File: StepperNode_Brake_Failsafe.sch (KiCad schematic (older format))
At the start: 2 parts

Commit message: Added Aux Prop Interface Sheet
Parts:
- added P?: CONN_01X02_2XMNT, symbol CONN_01X02_2XMNT
- added Q?: Q_NMOS_DGS, symbol Q_NMOS_DGS
- added RL?: Relay_DPDT, symbol Relay_DPDT
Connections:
- net labels added: WDT_GOOD
- wire segments 2 -> 4
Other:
- note added: "Brake 2 G210x\nEnable Link"
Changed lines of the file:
@@
 $Descr A3 16535 11693
 encoding utf-8
-Sheet 14 14
+Sheet 14 16
 Title "Brake Failsafe Control"
 Date ""
@@
 Text Notes 9850 2800 0    60   ~ 0
 G210x Active when\nRelay Energized
+$Comp
+L Q_NMOS_DGS Q?
+U 1 1 5753D96E
+P 8700 4250
+F 0 "Q?" H 9000 4300 50  0000 R CNN
+F 1 "Q_NMOS_DGS" H 9350 4200 50  0000 R CNN
+F 2 "" H 8900 4350 50  0000 C CNN
+F 3 "" H 8700 4250 50  0000 C CNN
+	1    8700 4250
+	1    0    0    -1
+$EndComp
+Text HLabel 6050 4200 0    60   Input ~ 0
+WDT_GOOD
+$Comp
+L CONN_01X02_2XMNT P?
+U 1 1 5753DAA1
+P 12200 5950
+F 0 "P?" H 12200 6100 50  0000 C CNN
+F 1 "CONN_01X02_2XMNT" V 12300 5950 50  0000 C CNN
+F 2 "" H 12200 5950 50  0000 C CNN
+F 3 "" H 12200 5950 50  0000 C CNN
+	1    12200 5950
+	1    0    0    -1
+$EndComp
+Text Notes 12550 5950 0    60   ~ 0
+Brake 2 G210x\nEnable Link
+$Comp
+L Relay_DPDT RL?
+U 1 1 5753DAA8
+P 9100 6450
+F 0 "RL?" H 9500 7250 60  0000 C CNN
+F 1 "Relay_DPDT" H 9500 6400 60  0000 C CNN
+F 2 "" H 9100 6450 60  0000 C CNN
+F 3 "" H 9100 6450 60  0000 C CNN
+	1    9100 6450
+	1    0    0    -1
+$EndComp
+Wire Wire Line
+	10100 6000 12000 6000
+Wire Wire Line
+	12000 5900 10100 5900
+Text Notes 9850 5500 0    60   ~ 0
+G210x Active when\nRelay Energized
 $EndSCHEMATC

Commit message: Netlist top level
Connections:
- net labels added: PUSH_INTLK_A, PUSH_INTLK_B
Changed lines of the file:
@@
 Text Notes 9850 5500 0    60   ~ 0
 G210x Active when\nRelay Energized
+Text HLabel 5550 5100 0    60   Input ~ 0
+PUSH_INTLK_A
+Text HLabel 5550 5200 0    60   Input ~ 0
+PUSH_INTLK_B
 $EndSCHEMATC

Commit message: Updated node core connector pages and added interlocks.
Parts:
- removed Q?: Q_NMOS_DGS, symbol Q_NMOS_DGS
- removed RL?: Relay_DPDT, symbol Relay_DPDT
- added D?: 1N4004, symbol D
- added U?: NUD3124LT1G, symbol NUD3124LT1G
- added U? (x2): 74LVC1G32GW,125, symbol 74LVC1G32GW,125
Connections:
- net labels added: GNDD
- wire segments 4 -> 20
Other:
- note added: "If WDT or any Interlock is active then\nThe drive controllers always remain active.\nIn this mode a WDT fault can't cause loss of drive motors."
- note added: "Output is high when either\nInterlock is on"
- note added: "The purpose of this function is to:\n1. Ensure that if the WDT_GOOD signal goes low the drive controllers do not drop out if the interlock is enabled.\n2. Loss of either 24VA or 24VB will not cause the loss of an individual drive controller."
- note added: "Todo:\nPower RLY from redundant source."
- moved on the sheet: P?, RL?
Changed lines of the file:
@@
 L CONN_01X02_2XMNT P?
 U 1 1 575559F0
-P 12200 3250
-F 0 "P?" H 12200 3400 50  0000 C CNN
-F 1 "CONN_01X02_2XMNT" V 12300 3250 50  0000 C CNN
-F 2 "" H 12200 3250 50  0000 C CNN
-F 3 "" H 12200 3250 50  0000 C CNN
-	1    12200 3250
+P 12350 4250
+F 0 "P?" H 12350 4400 50  0000 C CNN
+F 1 "CONN_01X02_2XMNT" V 12450 4250 50  0000 C CNN
+F 2 "" H 12350 4250 50  0000 C CNN
+F 3 "" H 12350 4250 50  0000 C CNN
+	1    12350 4250
 	1    0    0    -1
 $EndComp
-Text Notes 12550 3250 0    60   ~ 0
+Text Notes 12700 4250 0    60   ~ 0
 Brake 1 G210x\nEnable Link
 $Comp
 L Relay_DPDT RL?
 U 1 1 57555A31
-P 9100 3750
-F 0 "RL?" H 9500 4550 60  0000 C CNN
-F 1 "Relay_DPDT" H 9500 3700 60  0000 C CNN
-F 2 "" H 9100 3750 60  0000 C CNN
-F 3 "" H 9100 3750 60  0000 C CNN
-	1    9100 3750
+P 9250 4750
+F 0 "RL?" H 9650 5550 60  0000 C CNN
+F 1 "Relay_DPDT" H 9650 4700 60  0000 C CNN
+F 2 "" H 9250 4750 60  0000 C CNN
+F 3 "" H 9250 4750 60  0000 C CNN
+	1    9250 4750
 	1    0    0    -1
 $EndComp
 Wire Wire Line
-	10100 3300 12000 3300
+	10250 4300 12150 4300
 Wire Wire Line
-	12000 3200 10100 3200
-Text Notes 9850 2800 0    60   ~ 0
+	12150 4200 10250 4200
+Text Notes 10000 3800 0    60   ~ 0
 G210x Active when\nRelay Energized
-$Comp
-L Q_NMOS_DGS Q?
-U 1 1 5753D96E
-P 8700 4250
-F 0 "Q?" H 9000 4300 50  0000 R CNN
-F 1 "Q_NMOS_DGS" H 9350 4200 50  0000 R CNN
-F 2 "" H 8900 4350 50  0000 C CNN
-F 3 "" H 8700 4250 50  0000 C CNN
-	1    8700 4250
-	1    0    0    -1
-$EndComp
-Text HLabel 6050 4200 0    60   Input ~ 0
+Text HLabel 5650 4150 0    60   Input ~ 0
 WDT_GOOD
 $Comp
 L CONN_01X02_2XMNT P?
 U 1 1 5753DAA1
-P 12200 5950
-F 0 "P?" H 12200 6100 50  0000 C CNN
-F 1 "CONN_01X02_2XMNT" V 12300 5950 50  0000 C CNN
-F 2 "" H 12200 5950 50  0000 C CNN
-F 3 "" H 12200 5950 50  0000 C CNN
-	1    12200 5950
+P 12300 5350
+F 0 "P?" H 12300 5500 50  0000 C CNN
+F 1 "CONN_01X02_2XMNT" V 12400 5350 50  0000 C CNN
+F 2 "" H 12300 5350 50  0000 C CNN
+F 3 "" H 12300 5350 50  0000 C CNN
+	1    12300 5350
 	1    0    0    -1
 $EndComp
-Text Notes 12550 5950 0    60   ~ 0
+Text Notes 12650 5350 0    60   ~ 0
 Brake 2 G210x\nEnable Link
+Text HLabel 4150 5400 0    60   Input ~ 0
+PUSH_INTLK_A
+Text HLabel 4150 5600 0    60   Input ~ 0
+PUSH_INTLK_B
 $Comp
-L Relay_DPDT RL?
-U 1 1 5753DAA8
-P 9100 6450
-F 0 "RL?" H 9500 7250 60  0000 C CNN
-F 1 "Relay_DPDT" H 9500 6400 60  0000 C CNN
-F 2 "" H 9100 6450 60  0000 C CNN
-F 3 "" H 9100 6450 60  0000 C CNN
-	1    9100 6450
+L NUD3124LT1G U?
+U 1 1 575D735B
+P 8750 5100
+F 0 "U?" H 8750 5200 60  0000 C CNN
+F 1 "NUD3124LT1G" H 9450 4450 60  0000 C CNN
+F 2 "" H 8750 5100 60  0000 C CNN
+F 3 "" H 8750 5100 60  0000 C CNN
+	1    8750 5100
 	1    0    0    -1
 $EndComp
 Wire Wire Line
-	10100 6000 12000 6000
+	9050 4550 9050 4900
+$Comp
+L GNDD #PWR?
+U 1 1 575D769D
+P 9050 5900
+F 0 "#PWR?" H 9050 5650 50  0001 C CNN
+F 1 "GNDD" H 9050 5750 50  0000 C CNN
+F 2 "" H 9050 5900 50  0000 C CNN
+F 3 "" H 9050 5900 50  0000 C CNN
+	1    9050 5900
+	1    0    0    -1
+$EndComp
+$Comp
+L D D?
+U 1 1 575D7CC9
+P 8750 4350
+F 0 "D?" H 8750 4450 50  0000 C CNN
+F 1 "1N4004" H 8750 4250 50  0000 C CNN
+F 2 "" H 8750 4350 50  0000 C CNN
+F 3 "" H 8750 4350 50  0000 C CNN
+	1    8750 4350
+	0    1    1    0
+$EndComp
 Wire Wire Line
-	12000 5900 10100 5900
-Text Notes 9850 5500 0    60   ~ 0
-G210x Active when\nRelay Energized
-Text HLabel 5550 5100 0    60   Input ~ 0
-PUSH_INTLK_A
-Text HLabel 5550 5200 0    60   Input ~ 0
-PUSH_INTLK_B
+	8750 4150 9050 4150
+Wire Wire Line
+	8750 4150 8750 4200
+Wire Wire Line
+	9050 4550 8750 4550
+Wire Wire Line
+	8750 4550 8750 4500
+Text Notes 3800 1650 0    60   ~ 0
+The purpose of this function is to:\n1. Ensure that if the WDT_GOOD signal goes low the drive controllers do not drop out if the interlock is enabled.\n2. Loss of either 24VA or 24VB will not cause the loss of an individual drive controller.
+Wire Wire Line
+	10250 4550 11250 4550
+Wire Wire Line
+	11250 4550 11250 5300
+Wire Wire Line
+	11250 5300 12100 5300
+Wire Wire Line
+	10250 4650 11150 4650
+Wire Wire Line
+	11150 4650 11150 5400
+Wire Wire Line
+	11150 5400 12100 5400
+$Comp
+L 74LVC1G32GW,125 U?
+U 1 1 575DA2FF
+P 5200 5250
+F 0 "U?" H 5200 5400 60  0000 C CNN
+F 1 "74LVC1G32GW,125" H 6000 4600 60  0000 C CNN
+F 2 "" H 5200 5250 60  0000 C CNN
+F 3 "" H 5200 5250 60  0000 C CNN
+	1    5200 5250
+	1    0    0    -1
+$EndComp
+Wire Wire Line
+	5000 5400 4150 5400
+Wire Wire Line
+	4150 5600 5000 5600
+$Comp
+L GNDD #PWR?
+U 1 1 575DA88C
+P 5500 6000
+F 0 "#PWR?" H 5500 5750 50  0001 C CNN
+F 1 "GNDD" H 5500 5850 50  0000 C CNN
+F 2 "" H 5500 6000 50  0000 C CNN
+F 3 "" H 5500 6000 50  0000 C CNN
+	1    5500 6000
+	1    0    0    -1
+$EndComp
+Text Notes 4950 6450 0    60   ~ 0
+Output is high when either\nInterlock is on
+$Comp
+L 74LVC1G32GW,125 U?
+U 1 1 575DAC72
+P 6900 5150
+F 0 "U?" H 6900 5300 60  0000 C CNN
+F 1 "74LVC1G32GW,125" H 7700 4500 60  0000 C CNN
+F 2 "" H 6900 5150 60  0000 C CNN
+F 3 "" H 6900 5150 60  0000 C CNN
+	1    6900 5150
+	1    0    0    -1
+$EndComp
+$Comp
+L GNDD #PWR?
+U 1 1 575DAC78
+P 7200 5900
+F 0 "#PWR?" H 7200 5650 50  0001 C CNN
+F 1 "GNDD" H 7200 5750 50  0000 C CNN
+F 2 "" H 7200 5900 50  0000 C CNN
+F 3 "" H 7200 5900 50  0000 C CNN
+	1    7200 5900
+	1    0    0    -1
+$EndComp
+Wire Wire Line
+	5950 5500 6700 5500
+Wire Wire Line
+	6700 5300 6350 5300
+Wire Wire Line
+	6350 5300 6350 4150
+Wire Wire Line
+	6350 4150 5650 4150
+Wire Wire Line
+	7650 5400 8550 5400
+Text Notes 7000 6500 0    60   ~ 0
+If WDT or any Interlock is active then\nThe drive controllers always remain active.\nIn this mode a WDT fault can't cause loss of drive motors.
+Text Notes 9000 3900 1    60   ~ 0
+Todo:\nPower RLY from redundant source.
 $EndSCHEMATC

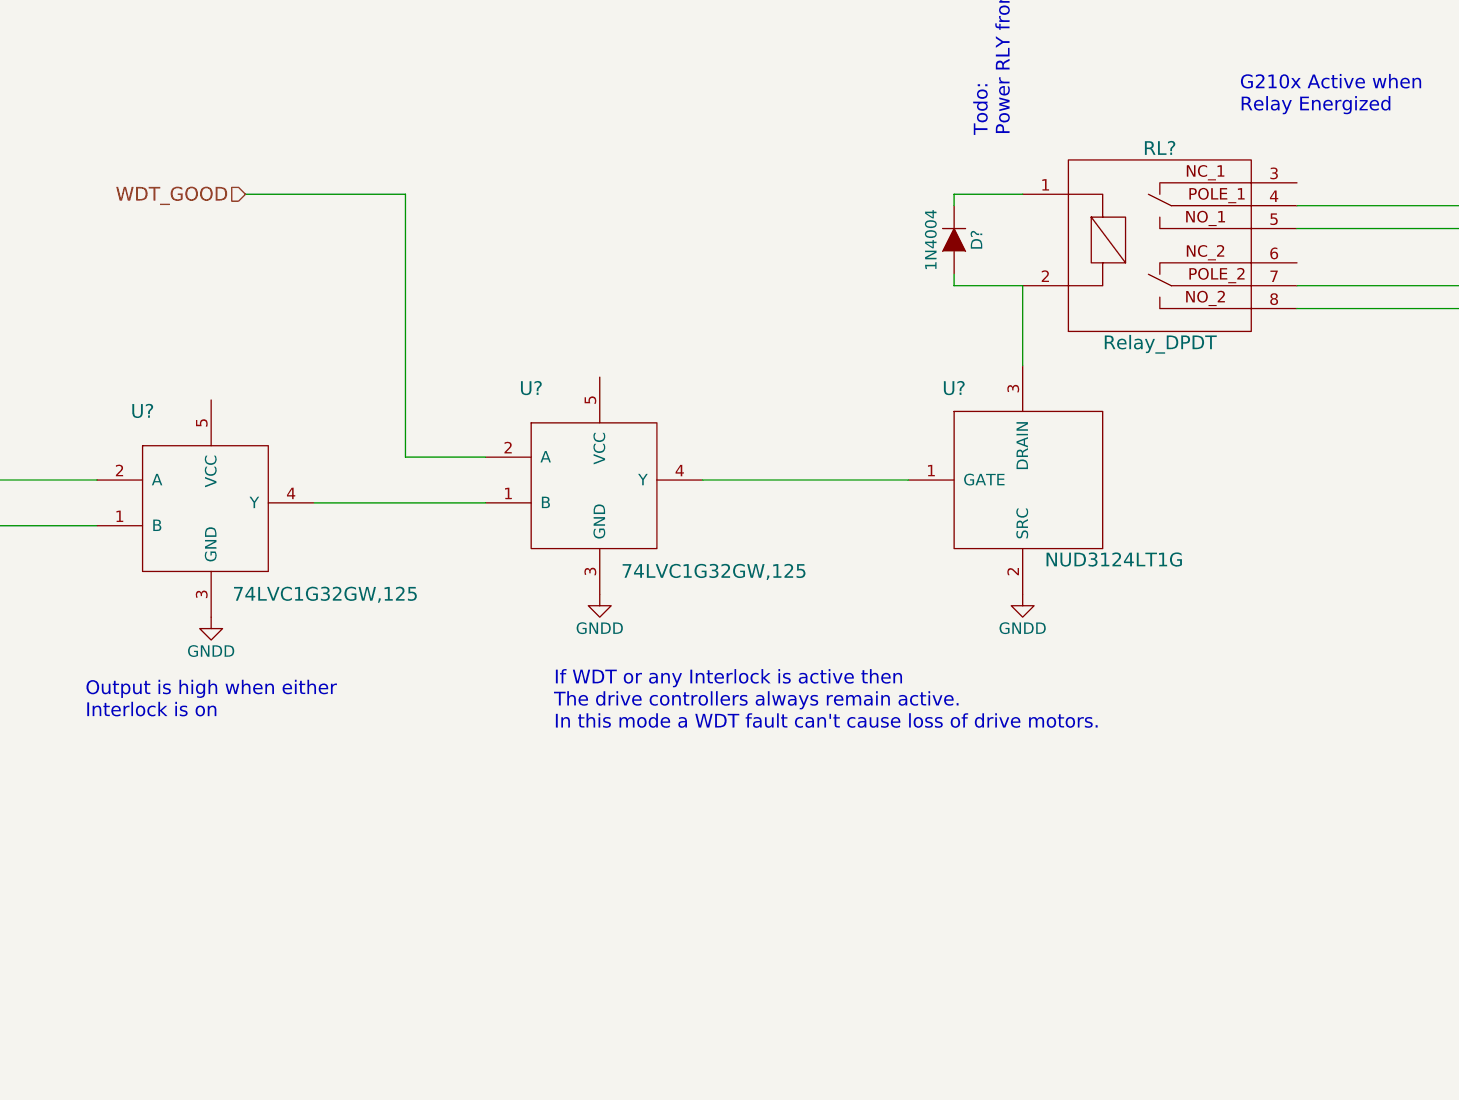
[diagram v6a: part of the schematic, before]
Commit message: Update DAC's and routed gimbal position to MCU direct.
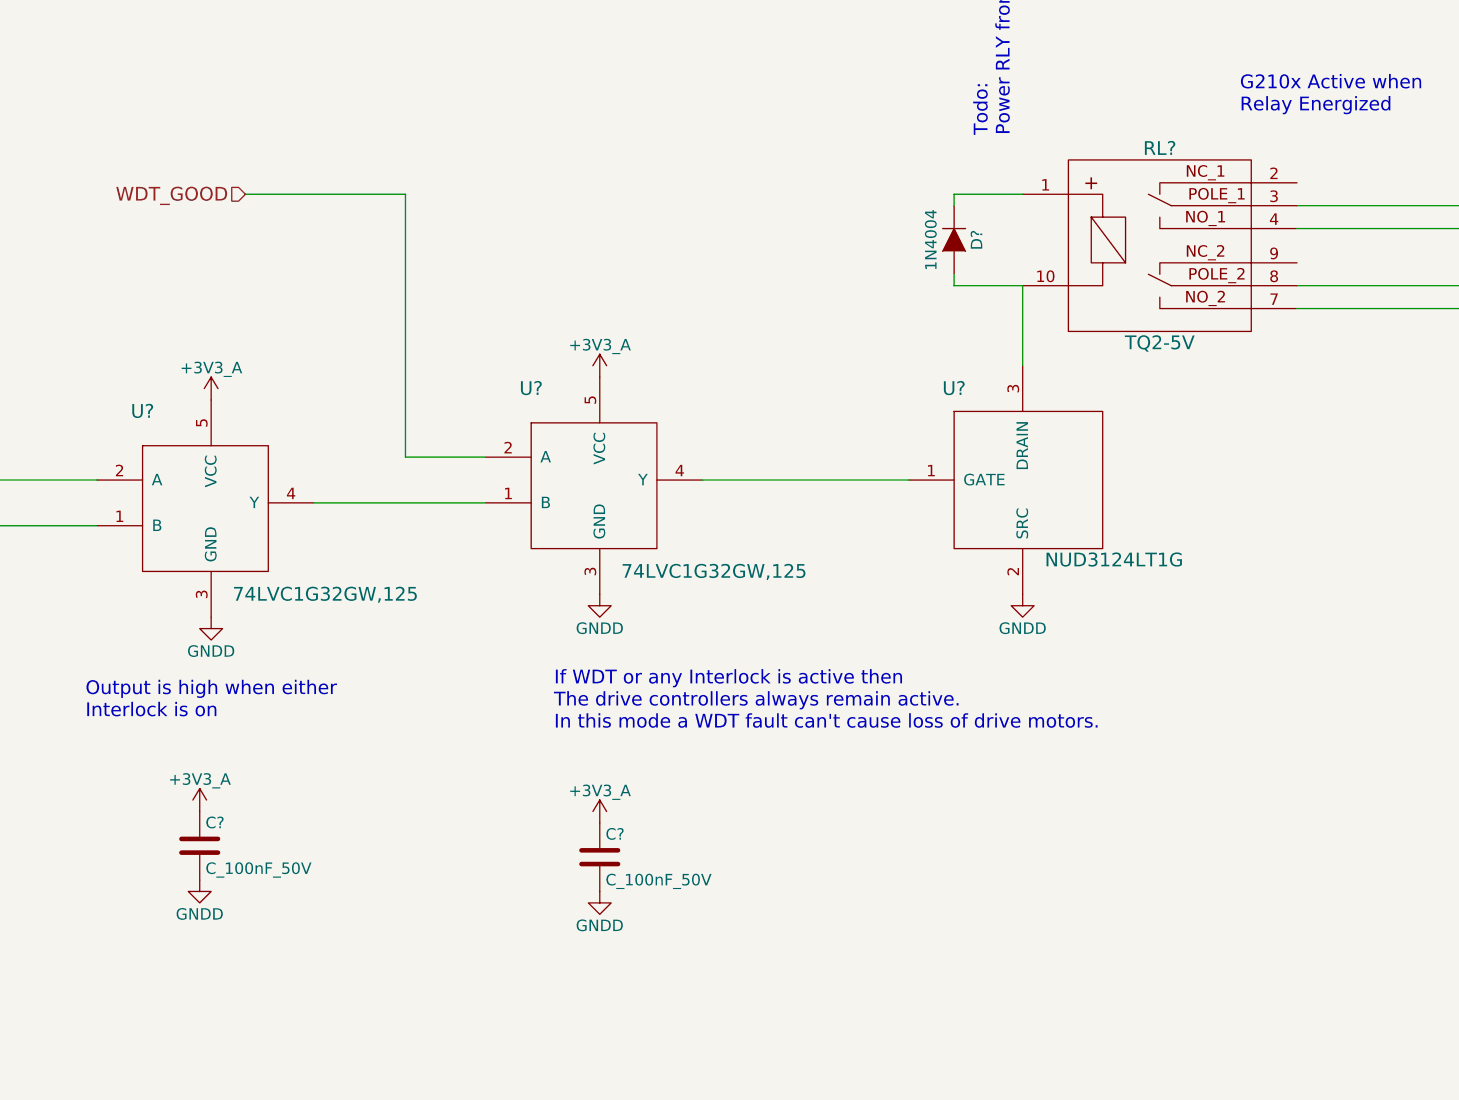
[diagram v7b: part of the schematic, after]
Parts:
- removed RL?: Relay_DPDT, symbol Relay_DPDT
- removed U?: NUD3124LT1G, symbol NUD3124LT1G
- removed U? (x2): 74LVC1G32GW,125, symbol 74LVC1G32GW,125
- added C? (x2): C_100nF_50V, RLOOP_FOOTPRINTS:rLoop_C_0603, symbol C_100nF_50V
- added RL?: TQ2-5V, symbol TQ2-5V
- added U?: NUD3124LT1G, RLOOP_FOOTPRINTS:rLoop_SOT23, symbol NUD3124LT1G
- added U? (x2): 74LVC1G32GW,125, RLOOP_FOOTPRINTS:rLoop_SOT353, symbol 74LVC1G32GW,125
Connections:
- net GNDD: now also C?.2, C?.2, U?.2 (SRC), U?.3 (GND), U?.3 (GND)
- net PUSH_INTLK_A: now also U?.2 (A)
- net PUSH_INTLK_B: now also U?.1 (B)
- net WDT_GOOD: now also U?.2 (A)
- net at P?.1 (P1): now also RL?.8
- net at P?.2 (P2): now also RL?.7
- net at P?.1 (P1): now also RL?.3
- net at P?.2 (P2): now also RL?.4
- net at D?.1 (K): now also RL?.1
- net at D?.2 (A): now also RL?.10, U?.3 (DRAIN)
- new net: U?.1 (GATE), U?.4 (Y)
- new net: U?.1 (B), U?.4 (Y)
- new net +3V3: C?.1, C?.1, U?.5 (VCC), U?.5 (VCC)
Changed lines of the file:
@@
 $Descr A3 16535 11693
 encoding utf-8
-Sheet 13 15
+Sheet 8 15
 Title "Brake Failsafe Control"
 Date ""
@@
 Text Notes 12700 4250 0    60   ~ 0
 Brake 1 G210x\nEnable Link
-$Comp
-L Relay_DPDT RL?
-U 1 1 57555A31
-P 9250 4750
-F 0 "RL?" H 9650 5550 60  0000 C CNN
-F 1 "Relay_DPDT" H 9650 4700 60  0000 C CNN
-F 2 "" H 9250 4750 60  0000 C CNN
-F 3 "" H 9250 4750 60  0000 C CNN
-	1    9250 4750
-	1    0    0    -1
-$EndComp
 Wire Wire Line
 	10250 4300 12150 4300
@@
 Text HLabel 4150 5600 0    60   Input ~ 0
 PUSH_INTLK_B
-$Comp
-L NUD3124LT1G U?
-U 1 1 575D735B
-P 8750 5100
-F 0 "U?" H 8750 5200 60  0000 C CNN
-F 1 "NUD3124LT1G" H 9450 4450 60  0000 C CNN
-F 2 "" H 8750 5100 60  0000 C CNN
-F 3 "" H 8750 5100 60  0000 C CNN
-	1    8750 5100
-	1    0    0    -1
-$EndComp
 Wire Wire Line
 	9050 4550 9050 4900
@@
 Wire Wire Line
 	11150 5400 12100 5400
-$Comp
-L 74LVC1G32GW,125 U?
-U 1 1 575DA2FF
-P 5200 5250
-F 0 "U?" H 5200 5400 60  0000 C CNN
-F 1 "74LVC1G32GW,125" H 6000 4600 60  0000 C CNN
-F 2 "" H 5200 5250 60  0000 C CNN
-F 3 "" H 5200 5250 60  0000 C CNN
-	1    5200 5250
-	1    0    0    -1
-$EndComp
 Wire Wire Line
 	5000 5400 4150 5400
@@
 Output is high when either\nInterlock is on
 $Comp
-L 74LVC1G32GW,125 U?
-U 1 1 575DAC72
-P 6900 5150
-F 0 "U?" H 6900 5300 60  0000 C CNN
-F 1 "74LVC1G32GW,125" H 7700 4500 60  0000 C CNN
-F 2 "" H 6900 5150 60  0000 C CNN
-F 3 "" H 6900 5150 60  0000 C CNN
-	1    6900 5150
-	1    0    0    -1
-$EndComp
-$Comp
 L GNDD #PWR?
 U 1 1 575DAC78
@@
 Text Notes 9000 3900 1    60   ~ 0
 Todo:\nPower RLY from redundant source.
+$Comp
+L NUD3124LT1G U?
+U 1 1 575A7BBF
+P 8750 5100
+F 0 "U?" H 8750 5200 60  0000 C CNN
+F 1 "NUD3124LT1G" H 9450 4450 60  0000 C CNN
+F 2 "RLOOP_FOOTPRINTS:rLoop_SOT23" H 8650 5100 60  0001 C CNN
+F 3 "" H 8750 5100 60  0000 C CNN
+	1    8750 5100
+	1    0    0    -1
+$EndComp
+$Comp
+L 74LVC1G32GW,125 U?
+U 1 1 575A8256
+P 5200 5250
+F 0 "U?" H 5200 5400 60  0000 C CNN
+F 1 "74LVC1G32GW,125" H 6000 4600 60  0000 C CNN
+F 2 "RLOOP_FOOTPRINTS:rLoop_SOT353" H 5100 5300 60  0001 C CNN
+F 3 "" H 5200 5250 60  0000 C CNN
+	1    5200 5250
+	1    0    0    -1
+$EndComp
+$Comp
+L +3V3_A #PWR?
+U 1 1 575A85D8
+P 5500 5050
+F 0 "#PWR?" H 5500 4900 50  0001 C CNN
+F 1 "+3V3_A" H 5500 5190 50  0000 C CNN
+F 2 "" H 5500 5050 60  0000 C CNN
+F 3 "" H 5500 5050 60  0000 C CNN
+	1    5500 5050
+	1    0    0    -1
+$EndComp
+$Comp
+L +3V3_A #PWR?
+U 1 1 575A85F8
+P 7200 4950
+F 0 "#PWR?" H 7200 4800 50  0001 C CNN
+F 1 "+3V3_A" H 7200 5090 50  0000 C CNN
+F 2 "" H 7200 4950 60  0000 C CNN
+F 3 "" H 7200 4950 60  0000 C CNN
+	1    7200 4950
+	1    0    0    -1
+$EndComp
+$Comp
+L C_100nF_50V C?
+U 1 1 575A8625
+P 5450 7000
+F 0 "C?" H 5475 7100 50  0000 L CNN
+F 1 "C_100nF_50V" H 5475 6900 50  0000 L CNN
+F 2 "RLOOP_FOOTPRINTS:rLoop_C_0603" H 5488 6850 50  0001 C CNN
+F 3 "" H 5450 7000 50  0000 C CNN
+	1    5450 7000
+	1    0    0    -1
+$EndComp
+$Comp
+L GNDD #PWR?
+U 1 1 575A86D0
+P 5450 7150
+F 0 "#PWR?" H 5450 6900 50  0001 C CNN
+F 1 "GNDD" H 5450 7000 50  0000 C CNN
+F 2 "" H 5450 7150 50  0000 C CNN
+F 3 "" H 5450 7150 50  0000 C CNN
+	1    5450 7150
+	1    0    0    -1
+$EndComp
+$Comp
+L +3V3_A #PWR?
+U 1 1 575A86E0
+P 5450 6850
+F 0 "#PWR?" H 5450 6700 50  0001 C CNN
+F 1 "+3V3_A" H 5450 6990 50  0000 C CNN
+F 2 "" H 5450 6850 60  0000 C CNN
+F 3 "" H 5450 6850 60  0000 C CNN
+	1    5450 6850
+	1    0    0    -1
+$EndComp
+$Comp
+L C_100nF_50V C?
+U 1 1 575A891A
+P 7200 7050
+F 0 "C?" H 7225 7150 50  0000 L CNN
+F 1 "C_100nF_50V" H 7225 6950 50  0000 L CNN
+F 2 "RLOOP_FOOTPRINTS:rLoop_C_0603" H 7238 6900 50  0001 C CNN
+F 3 "" H 7200 7050 50  0000 C CNN
+	1    7200 7050
+	1    0    0    -1
+$EndComp
+$Comp
+L GNDD #PWR?
+U 1 1 575A8920
+P 7200 7200
+F 0 "#PWR?" H 7200 6950 50  0001 C CNN
+F 1 "GNDD" H 7200 7050 50  0000 C CNN
+F 2 "" H 7200 7200 50  0000 C CNN
+F 3 "" H 7200 7200 50  0000 C CNN
+	1    7200 7200
+	1    0    0    -1
+$EndComp
+$Comp
+L +3V3_A #PWR?
+U 1 1 575A8926
+P 7200 6900
+F 0 "#PWR?" H 7200 6750 50  0001 C CNN
+F 1 "+3V3_A" H 7200 7040 50  0000 C CNN
+F 2 "" H 7200 6900 60  0000 C CNN
+F 3 "" H 7200 6900 60  0000 C CNN
+	1    7200 6900
+	1    0    0    -1
+$EndComp
+$Comp
+L 74LVC1G32GW,125 U?
+U 1 1 575A8AA1
+P 6900 5150
+F 0 "U?" H 6900 5300 60  0000 C CNN
+F 1 "74LVC1G32GW,125" H 7700 4500 60  0000 C CNN
+F 2 "RLOOP_FOOTPRINTS:rLoop_SOT353" H 6800 5200 60  0001 C CNN
+F 3 "" H 6900 5150 60  0000 C CNN
+	1    6900 5150
+	1    0    0    -1
+$EndComp
+$Comp
+L TQ2-5V RL?
+U 1 1 575A2812
+P 9250 4000
+F 0 "RL?" H 9650 4050 60  0000 C CNN
+F 1 "TQ2-5V" H 9650 3200 60  0000 C CNN
+F 2 "" H 9250 3250 60  0000 C CNN
+F 3 "" H 9250 3250 60  0000 C CNN
+	1    9250 4000
+	1    0    0    -1
+$EndComp
 $EndSCHEMATC
